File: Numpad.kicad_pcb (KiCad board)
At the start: 2 copper layers, 76.2 x 88.9 mm, 102 parts, among them J1 USB_C_Receptacle_USB2.0, J3 AVR-ISP-6, Q101 DMN2041L, Q2 DMN2041L, SW10 SW_Push, SW11 SW_Push, SW12 SW_Push, SW13 SW_Push, SW14 SW_Push, SW15 SW_Push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

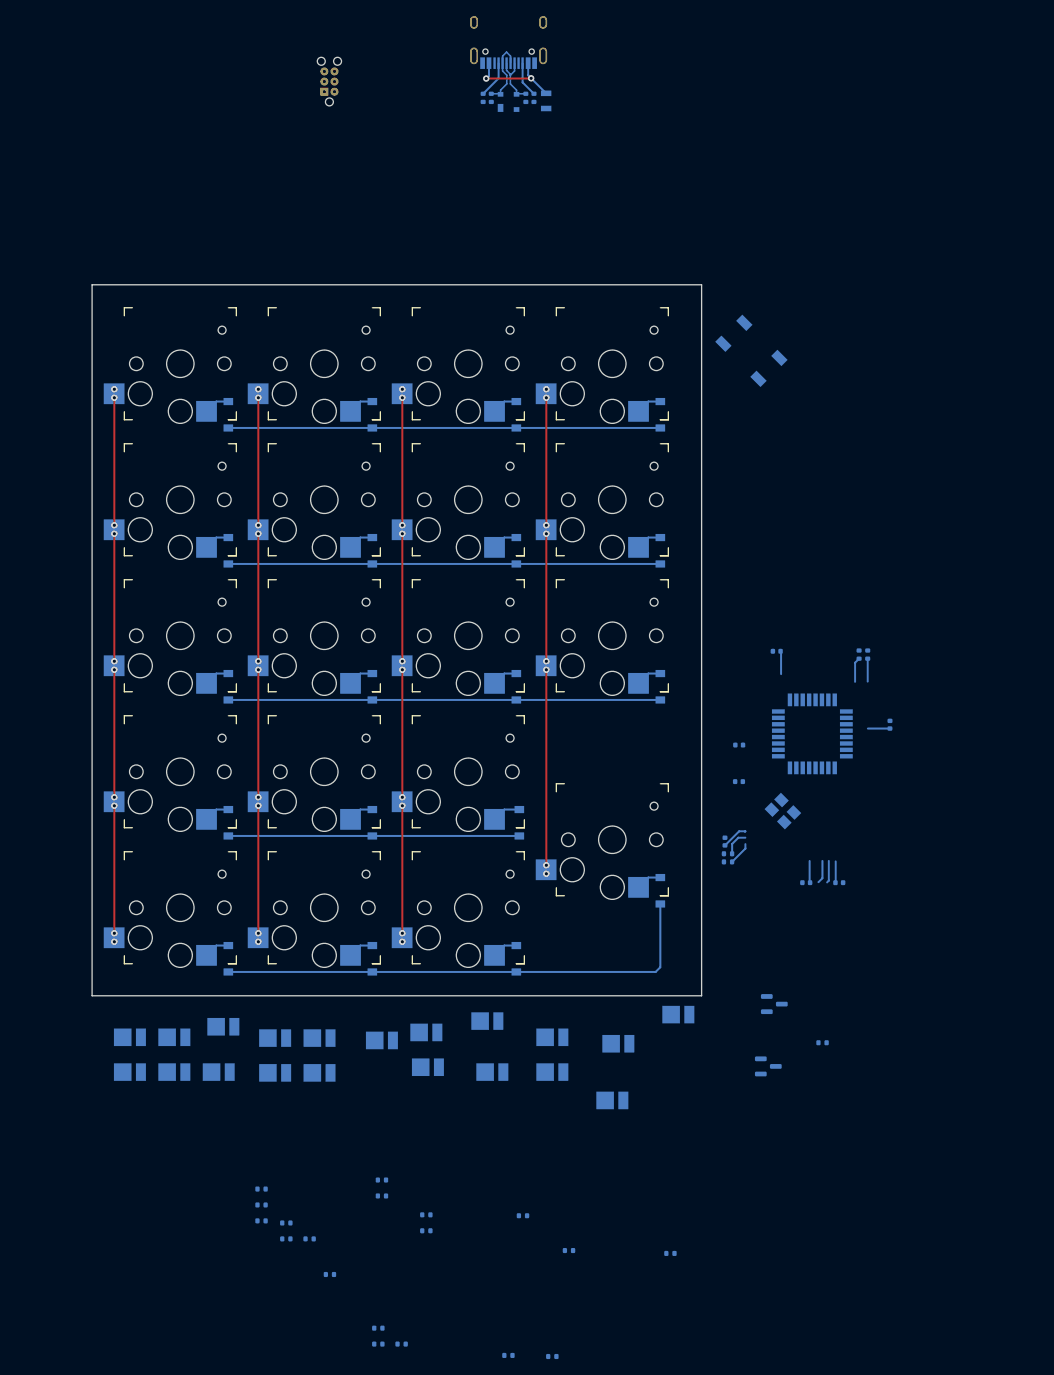
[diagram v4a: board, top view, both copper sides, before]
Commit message: swapped leds to rgb leds, and added a whole lot of routing
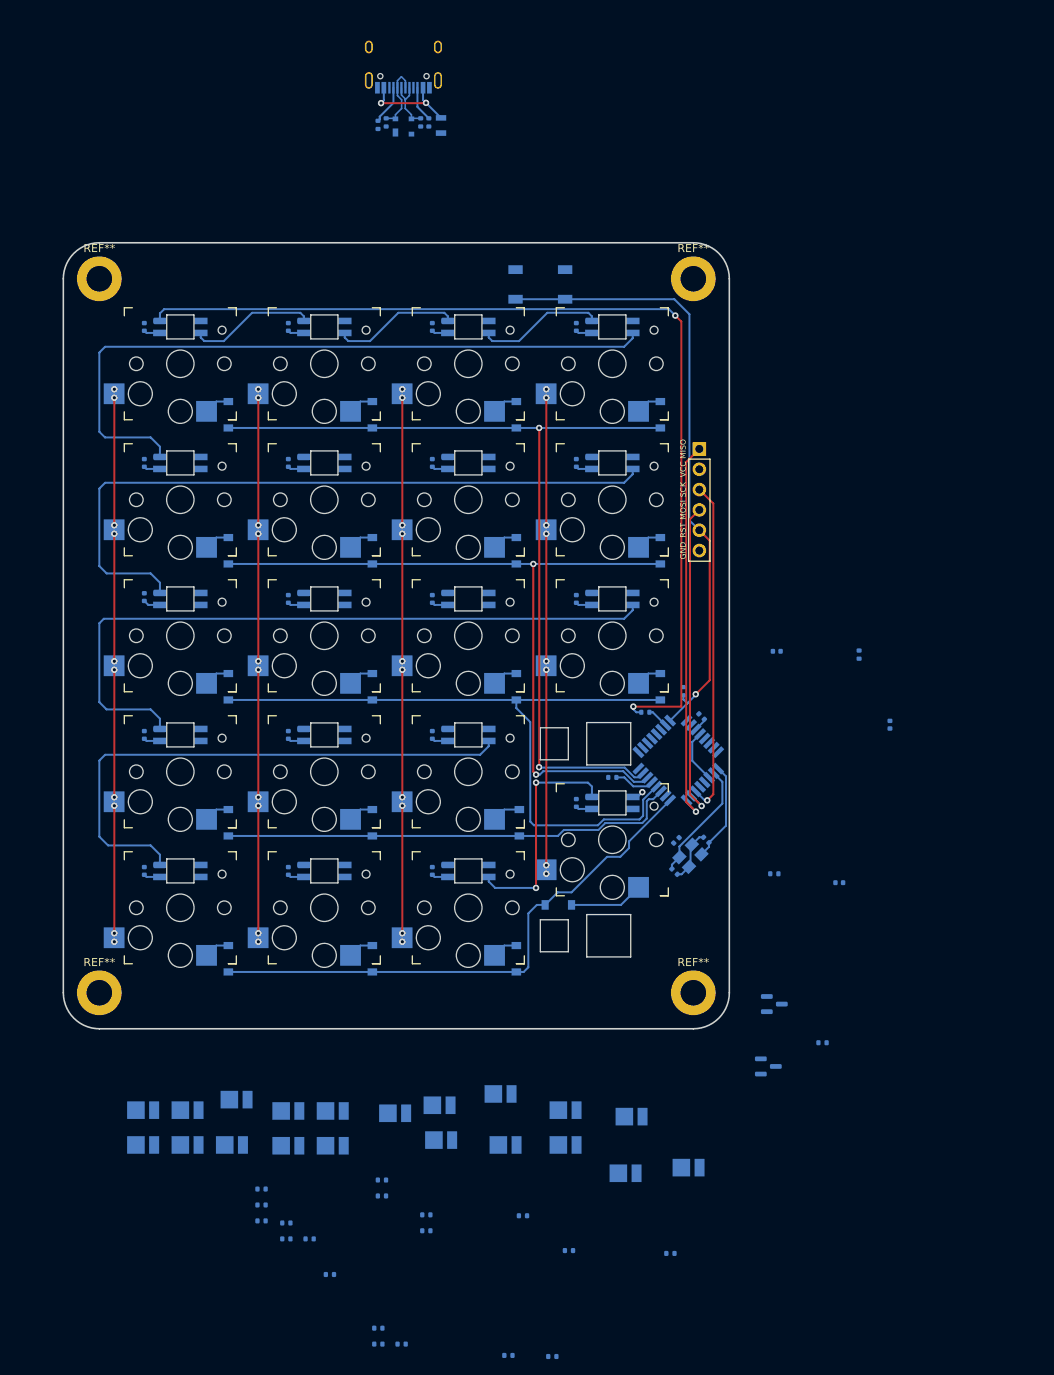
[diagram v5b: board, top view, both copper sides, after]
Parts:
- added C10: 100nF, Capacitor_SMD:C_0402_1005Metric, B.Cu at (103.5, 29.4)
- added C11: 100nF, Capacitor_SMD:C_0402_1005Metric, B.Cu at (121.5, 29.4)
- added C12: 100nF, Capacitor_SMD:C_0402_1005Metric, B.Cu at (67.5, 46.4)
- added C13: 100nF, Capacitor_SMD:C_0402_1005Metric, B.Cu at (85.5, 46.4)
- added C14: 100nF, Capacitor_SMD:C_0402_1005Metric, B.Cu at (103.5, 46.4)
- added C15: 100nF, Capacitor_SMD:C_0402_1005Metric, B.Cu at (121.5, 46.4)
- added C16: 100nF, Capacitor_SMD:C_0402_1005Metric, B.Cu at (67.5, 63.2)
- added C17: 100nF, Capacitor_SMD:C_0402_1005Metric, B.Cu at (85.5, 63.4)
- added C18: 100nF, Capacitor_SMD:C_0402_1005Metric, B.Cu at (103.5, 63.4)
- added C19: 100nF, Capacitor_SMD:C_0402_1005Metric, B.Cu at (121.5, 63.4)
- added C20: 100nF, Capacitor_SMD:C_0402_1005Metric, B.Cu at (67.5, 80.4)
- added C21: 100nF, Capacitor_SMD:C_0402_1005Metric, B.Cu at (85.5, 80.4)
- added C22: 100nF, Capacitor_SMD:C_0402_1005Metric, B.Cu at (103.5, 80.4)
- added C23: 100nF, Capacitor_SMD:C_0402_1005Metric, B.Cu at (121.5, 88.9)
- added C24: 100nF, Capacitor_SMD:C_0402_1005Metric, B.Cu at (67.5, 97.4)
- added C25: 100nF, Capacitor_SMD:C_0402_1005Metric, B.Cu at (85.5, 97.4)
- added C26: 100nF, Capacitor_SMD:C_0402_1005Metric, B.Cu at (103.5, 97.4)
- added C8: 100nF, Capacitor_SMD:C_0402_1005Metric, B.Cu at (67.5, 29.4)
- added C9: 100nF, Capacitor_SMD:C_0402_1005Metric, B.Cu at (85.5, 29.4)
- added D20: SK6812MINI, Keebio-Parts:SK6812-MINI-E, B.Cu at (72.0, 29.4)
- added D22: SK6812MINI, Keebio-Parts:SK6812-MINI-E, B.Cu at (90.0, 29.4)
- added D23: SK6812MINI, Keebio-Parts:SK6812-MINI-E, B.Cu at (108.0, 29.4)
- added D24: SK6812MINI, Keebio-Parts:SK6812-MINI-E, B.Cu at (126.0, 29.4)
- added D25: SK6812MINI, Keebio-Parts:SK6812-MINI-E, B.Cu at (72.0, 46.4)
- added D26: SK6812MINI, Keebio-Parts:SK6812-MINI-E, B.Cu at (90.0, 46.4)
- added D27: SK6812MINI, Keebio-Parts:SK6812-MINI-E, B.Cu at (108.0, 46.4)
- added D28: SK6812MINI, Keebio-Parts:SK6812-MINI-E, B.Cu at (126.0, 46.4)
- added D29: SK6812MINI, Keebio-Parts:SK6812-MINI-E, B.Cu at (72.0, 63.4)
- added D30: SK6812MINI, Keebio-Parts:SK6812-MINI-E, B.Cu at (90.0, 63.4)
- added D31: SK6812MINI, Keebio-Parts:SK6812-MINI-E, B.Cu at (108.0, 63.4)
- added D32: SK6812MINI, Keebio-Parts:SK6812-MINI-E, B.Cu at (126.0, 63.4)
- added D33: SK6812MINI, Keebio-Parts:SK6812-MINI-E, B.Cu at (72.0, 80.4)
- added D34: SK6812MINI, Keebio-Parts:SK6812-MINI-E, B.Cu at (90.0, 80.4)
- added D35: SK6812MINI, Keebio-Parts:SK6812-MINI-E, B.Cu at (108.0, 80.4)
- added D36: SK6812MINI, Keebio-Parts:SK6812-MINI-E, B.Cu at (126.0, 88.9)
- added D37: SK6812MINI, Keebio-Parts:SK6812-MINI-E, B.Cu at (72.0, 97.4)
- added D38: SK6812MINI, Keebio-Parts:SK6812-MINI-E, B.Cu at (90.0, 97.4)
- added D39: SK6812MINI, Keebio-Parts:SK6812-MINI-E, B.Cu at (108.0, 97.4)
- added Kailh PG1350: Choc, Keebio-Parts:Kailh-Stabilizer-2u-Vert, F.Cu at (126.0, 93.5)
- added R1: 300, Resistor_SMD:R_0402_1005Metric, B.Cu at (130.1, 77.6)
- added REF**: MountingHole_3.2mm_M3_DIN965_Pad, MountingHole:MountingHole_3.2mm_M3_DIN965_Pad, F.Cu at (136.1, 23.4)
- added REF**: MountingHole_3.2mm_M3_DIN965_Pad, MountingHole:MountingHole_3.2mm_M3_DIN965_Pad, F.Cu at (61.9, 112.6)
- added REF**: MountingHole_3.2mm_M3_DIN965_Pad, MountingHole:MountingHole_3.2mm_M3_DIN965_Pad, F.Cu at (136.1, 112.6)
- added REF**: MountingHole_3.2mm_M3_DIN965_Pad, MountingHole:MountingHole_3.2mm_M3_DIN965_Pad, F.Cu at (61.9, 23.4)
- J3: footprint Keebio-Parts:ICSP_1.27mm -> Keebio-Parts:ICSP-Header
- moved J3 64.7 mm to (136.9, 44.7), turned to 180 degrees
- moved R34 35.4 mm to (126.0, 85.7), turned to 180 degrees
- moved SW_RESET1 27.7 mm to (117.0, 24.1), turned to 180 degrees
- moved C4 24.5 mm to (137.2, 78.1), turned to 135 degrees
- moved R23 21.1 mm to (134.9, 74.9), turned to -90 degrees
- moved D111 19.2 mm to (135.5, 134.5)
- moved C5 17.8 mm to (133.8, 97.5), turned to -45 degrees
- moved U1 17.1 mm to (134.2, 83.6), turned to 135 degrees
- moved R31 13.6 mm to (96.7, 4.14)
- moved D1 13.5 mm to (99.9, 4.34)
- moved F1 13.5 mm to (104.6, 4.21)
- moved J1 13.5 mm to (99.9, -4.55)
- moved R2 13.5 mm to (102.0, 3.83)
- moved R22 13.5 mm to (103.1, 3.83)
- moved R44 13.5 mm to (97.7, 3.83)
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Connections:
- U1 pad 10: ROW_1 -> unconnected-(U1-Pad10)
- U1 pad 11: ROW_0 -> ROW_1
- U1 pad 23: PWM -> Net-(U1-Pad23)
- U1 pad 9: unconnected-(U1-Pad9) -> ROW_0
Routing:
- net RGB: track 0.00 -> 122.6 mm, vias 0 -> 2
- net D25: track 0.00 -> 87.6 mm
- net D33: track 0.00 -> 87.6 mm
- net D29: track 0.00 -> 87.5 mm
- net RST: track 3.21 -> 77.6 mm, vias 0 -> 1
- net D37: track 0.00 -> 69.4 mm
- net ROW_4: track 54.0 -> 110.1 mm, vias 0 -> 2
- net MISO: track 0.00 -> 48.4 mm, vias 0 -> 1
- net SCLK: track 0.00 -> 41.8 mm, vias 0 -> 1
- net ROW_3: track 54.0 -> 95.4 mm, vias 0 -> 2
- net MOSI: track 0.00 -> 40.0 mm, vias 0 -> 1
- net ROW_2: track 54.0 -> 89.1 mm
- net Net-(D36-Pad3): track 0.00 -> 28.5 mm, vias 0 -> 2
- net +5V: track 11.9 -> 39.5 mm
- net ROW_1: track 36.4 -> 57.8 mm
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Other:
- board size 76.2 x 88.9 mm -> 83.2 x 98.2 mm

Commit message: some more routing and messing around with usb rcep
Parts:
- removed D101, D102, D103, D104, D105, D106, D107, D108, D109, D110, D111, D112, D113, D114, D115, D117, D118, D119, D120: LED, LED_SMD:LED_PLCC_2835
- removed Q101: DMN2041L, Package_TO_SOT_SMD:SOT-23
- removed R101, R102, R103, R104, R105, R106, R107, R108, R109, R110, R111, R112, R113, R114, R115, R117, R118, R119, R120: 470, Resistor_SMD:R_0402_1005Metric
- removed R121: 1k, Resistor_SMD:R_0402_1005Metric
- removed REF** (x4): MountingHole_3.2mm_M3_DIN965_Pad, MountingHole:MountingHole_3.2mm_M3_DIN965_Pad
- added H1: MountingHole, MountingHole:MountingHole_2.2mm_M2_DIN965_Pad, F.Cu at (61.9, 23.4)
- added H2: MountingHole, MountingHole:MountingHole_2.2mm_M2_DIN965_Pad, F.Cu at (136.1, 23.4)
- added H3: MountingHole, MountingHole:MountingHole_2.2mm_M2_DIN965_Pad, F.Cu at (61.9, 112.6)
- added H4: MountingHole, MountingHole:MountingHole_2.2mm_M2_DIN965_Pad, F.Cu at (136.1, 112.6)
- Kailh PG1350: footprint Keebio-Parts:Kailh-Stabilizer-2u-Vert -> Keebio-Parts:Kailh-PG1350-2u-Custom
- moved J1 26.3 mm to (99.0, 21.8)
- moved R2 0.24 mm to (102.3, 3.83)
- moved D1 0.24 mm to (100.1, 4.34)
- moved F1 0.24 mm to (104.8, 4.21)
- moved R22 0.24 mm to (103.3, 3.83)
- moved R31 0.24 mm to (97.0, 4.14)
- moved R44 0.24 mm to (98.0, 3.83)
- moved C16 0.23 mm to (67.5, 63.4)
- moved D33 0.11 mm to (72.0, 80.3)
- moved D34 0.11 mm to (90.0, 80.3)
- moved D35 0.11 mm to (108.0, 80.3)
- moved D37 0.11 mm to (72.0, 97.3)
- moved D38 0.11 mm to (90.0, 97.3)
- moved D39 0.11 mm to (108.0, 97.3)
- moved D25 0.11 mm to (72.0, 46.3)
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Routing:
- net Net-(D34-Pad1): track 0.00 -> 16.4 mm
- net Net-(D38-Pad1): track 0.00 -> 16.4 mm
- net Net-(D37-Pad1): track 0.00 -> 16.4 mm
- net Net-(D26-Pad1): track 0.00 -> 16.4 mm
- net Net-(D31-Pad1): track 0.00 -> 16.4 mm
- net Net-(D29-Pad1): track 0.00 -> 16.4 mm
- net Net-(D27-Pad1): track 0.00 -> 16.3 mm
- net Net-(D25-Pad1): track 0.00 -> 16.3 mm
- net Net-(D30-Pad1): track 0.00 -> 16.3 mm
- net Net-(D33-Pad1): track 0.00 -> 16.3 mm
- net VCC: track 12.4 -> 0.00 mm, vias 2 -> 0
- net D-: track 8.79 -> 1.19 mm
- net D+: track 7.32 -> 1.19 mm
- net Net-(J1-PadA5): track 4.93 -> 0.29 mm
- net Net-(J1-PadB5): track 4.42 -> 0.00 mm
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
